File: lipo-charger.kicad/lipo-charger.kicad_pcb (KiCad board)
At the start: 2 copper layers, 23 x 35 mm, 18 parts, among them J1 JST-PH2 Device, J3 JST-PH2 Bat, U1 MCP73831-2-OT, U2 XB6166IS

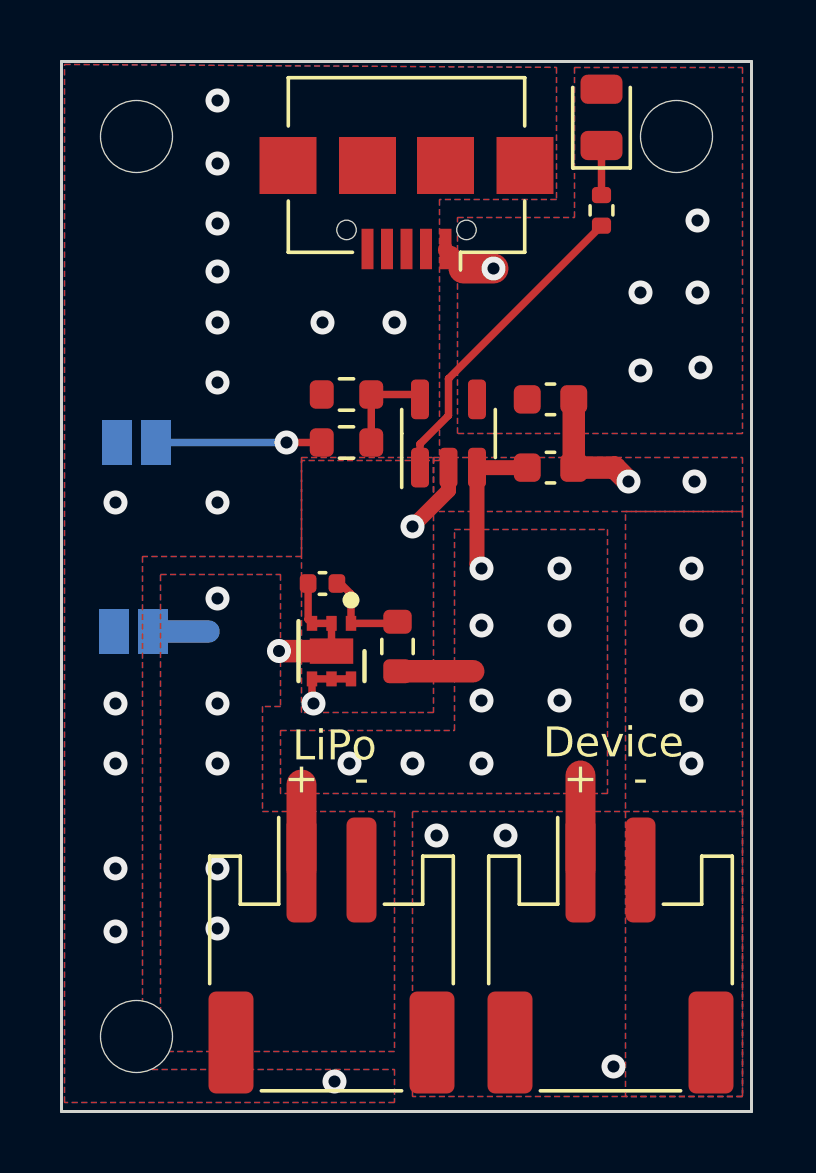
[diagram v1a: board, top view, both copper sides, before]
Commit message: Rev: 0.92: add (optional) switch for load
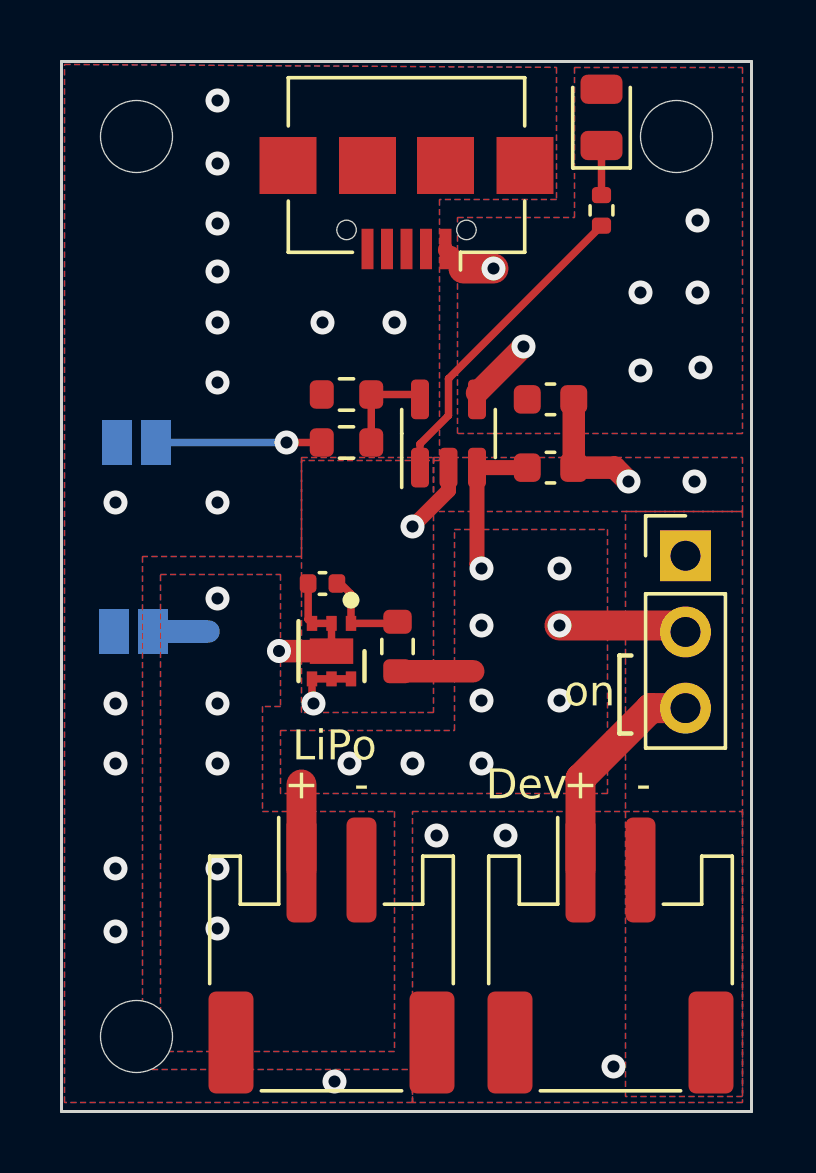
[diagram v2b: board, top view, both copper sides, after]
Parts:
- added SW1: SW_SPDT, Connector_PinHeader_2.54mm:PinHeader_1x03_P2.54mm_Vertical, F.Cu at (120.8, 116.5)
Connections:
- J1 pad 1: +BATT -> Net-(J1-Pad1)
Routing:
- net Net-(J1-Pad1): track 0.00 -> 7.52 mm
- net VBUS: track 1.90 -> 4.30 mm, vias 6 -> 7
- net +BATT: track 13.6 -> 14.8 mm
- net GND: vias 26 -> 22
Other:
- board text added: "Dev"
- board text added: "https://github.com/bablokb/ pcb-lipo-charger Rev: 0.92"
- board text added: "on"
- board text removed: "Device"
- board text removed: "https://github.com/bablokb/ pcb-lipo-charger Rev: 0.91"
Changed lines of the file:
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@@
   (net 11 "unconnected-(USB1-Pad3)")
   (net 12 "unconnected-(USB1-Pad2)")
+  (net 13 "Net-(J1-Pad1)")
+  (net 14 "unconnected-(SW1-Pad1)")
   (footprint "user:MountingHole_2.4mm_M2" (layer "F.Cu")
     (at 120.5 102.5)
@@
     )
   )
+  (footprint "Connector_PinHeader_2.54mm:PinHeader_1x03_P2.54mm_Vertical" (layer "F.Cu")
+    (at 120.8 116.475)
+    (descr "Through hole straight pin header, 1x03, 2.54mm pitch, single row")
+    (tags "Through hole pin header THT 1x03 2.54mm single row")
+    (property "Sheetfile" "lipo-charger.kicad_sch")
+    (property "Sheetname" "")
+    (attr through_hole)
+    (fp_text reference "SW1" (at 0 -2.33) (layer "F.SilkS") hide
+      (effects (font (size 1 1) (thickness 0.15)))
+    )
+    (fp_text value "SW_SPDT" (at 0 7.41) (layer "F.Fab")
+      (effects (font (size 1 1) (thickness 0.15)))
+    )
+    (fp_text user "${REFERENCE}" (at 0 2.54 90) (layer "F.Fab")
+      (effects (font (size 1 1) (thickness 0.15)))
+    )
+    (fp_line (start -1.33 6.41) (end 1.33 6.41) (layer "F.SilkS") (width 0.12))
+    (fp_line (start -1.33 -1.33) (end 0 -1.33) (layer "F.SilkS") (width 0.12))
+    (fp_line (start 1.33 1.27) (end 1.33 6.41) (layer "F.SilkS") (width 0.12))
+    (fp_line (start -1.33 0) (end -1.33 -1.33) (layer "F.SilkS") (width 0.12))
+    (fp_line (start -1.33 1.27) (end 1.33 1.27) (layer "F.SilkS") (width 0.12))
+    (fp_line (start -1.33 1.27) (end -1.33 6.41) (layer "F.SilkS") (width 0.12))
+    (fp_line (start 1.8 -1.8) (end -1.8 -1.8) (layer "F.CrtYd") (width 0.05))
+    (fp_line (start 1.8 6.85) (end 1.8 -1.8) (layer "F.CrtYd") (width 0.05))
+    (fp_line (start -1.8 6.85) (end 1.8 6.85) (layer "F.CrtYd") (width 0.05))
+    (fp_line (start -1.8 -1.8) (end -1.8 6.85) (layer "F.CrtYd") (width 0.05))
+    (fp_line (start -1.27 -0.635) (end -0.635 -1.27) (layer "F.Fab") (width 0.1))
+    (fp_line (start 1.27 -1.27) (end 1.27 6.35) (layer "F.Fab") (width 0.1))
+    (fp_line (start -0.635 -1.27) (end 1.27 -1.27) (layer "F.Fab") (width 0.1))
+    (fp_line (start 1.27 6.35) (end -1.27 6.35) (layer "F.Fab") (width 0.1))
+    (fp_line (start -1.27 6.35) (end -1.27 -0.635) (layer "F.Fab") (width 0.1))
+    (pad "1" thru_hole rect (at 0 0) (size 1.7 1.7) (drill 1) (layers *.Cu *.Mask)
+      (net 14 "unconnected-(SW1-Pad1)") (pinfunction "A") (pintype "passive+no_connect"))
+    (pad "2" thru_hole oval (at 0 2.54) (size 1.7 1.7) (drill 1) (layers *.Cu *.Mask)
+      (net 3 "+BATT") (pinfunction "B") (pintype "passive"))
+    (pad "3" thru_hole oval (at 0 5.08) (size 1.7 1.7) (drill 1) (layers *.Cu *.Mask)
+      (net 13 "Net-(J1-Pad1)") (pinfunction "C") (pintype "passive"))
+    (model "${KICAD6_3DMODEL_DIR}/Connector_PinHeader_2.54mm.3dshapes/PinHeader_1x03_P2.54mm_Vertical.wrl"
+      (offset (xyz 0 0 0))
+      (scale (xyz 1 1 1))
+      (rotate (xyz 0 0 0))
+    )
+  )
   (footprint "Resistor_SMD:R_0402_1005Metric" (layer "F.Cu")
     (at 118 104.9625 90)
@@
     (fp_line (start -3.95 -3.2) (end -3.15 -3.2) (layer "F.Fab") (width 0.1))
     (pad "1" smd roundrect (at -1 -2.85) (size 1 3.5) (layers "F.Cu" "F.Paste" "F.Mask") (roundrect_rratio 0.25)
-      (net 3 "+BATT") (pinfunction "Pin_1") (pintype "passive"))
+      (net 13 "Net-(J1-Pad1)") (pinfunction "Pin_1") (pintype "passive"))
     (pad "2" smd roundrect (at 1 -2.85) (size 1 3.5) (layers "F.Cu" "F.Paste" "F.Mask") (roundrect_rratio 0.25)
       (net 2 "GND") (pinfunction "Pin_2") (pintype "passive"))
@@
       (net 7 "Net-(JP1-Pad2)") (pinfunction "B") (pintype "passive"))
   )
+  (gr_line (start 118.6 119.8) (end 118.6 122.4) (layer "F.SilkS") (width 0.15))
+  (gr_line (start 118.6 122.4) (end 119 122.4) (layer "F.SilkS") (width 0.15))
+  (gr_line (start 118.6 119.8) (end 119 119.8) (layer "F.SilkS") (width 0.15))
   (gr_line (start 100 100) (end 123 100) (layer "Edge.Cuts") (width 0.1))
   (gr_line (start 123 100) (end 123 135) (layer "Edge.Cuts") (width 0.1))
   (gr_line (start 100 135) (end 100 100) (layer "Edge.Cuts") (width 0.1))
   (gr_line (start 123 135) (end 100 135) (layer "Edge.Cuts") (width 0.1))
-  (gr_text "https://github.com/bablokb/\n  pcb-lipo-charger\nRev: 0.91" (at 121.8 106.2) (layer "B.SilkS")
+  (gr_text "https://github.com/bablokb/\n  pcb-lipo-charger\nRev: 0.92" (at 121.8 106.2) (layer "B.SilkS")
     (effects (font (size 0.9 0.9) (thickness 0.15)) (justify left mirror))
   )
@@
     (effects (font (size 1 1) (thickness 0.15)) (justify left mirror))
   )
-  (gr_text "I charge: 200mA\nI fast:    500mA\n\nI load: 900mA max" (at 121.7 118.2) (layer "B.SilkS")
+  (gr_text "I charge: 200mA\nI fast:    500mA\n\nI load: 900mA max" (at 118.9 118.3) (layer "B.SilkS")
     (effects (font (size 1 1) (thickness 0.15)) (justify left mirror))
   )
-  (gr_text "+" (at 108 123.9) (layer "F.SilkS")
+  (gr_text "+" (at 108 124.1) (layer "F.SilkS")
     (effects (font (size 1 1) (thickness 0.15)))
   )
@@
     (effects (font (size 1 1) (thickness 0.15)))
   )
-  (gr_text "Device" (at 118.4 122.7) (layer "F.SilkS")
+  (gr_text "Dev" (at 115.5 124.1) (layer "F.SilkS")
     (effects (font (size 1 1) (thickness 0.15)))
   )
-  (gr_text "-" (at 119.3 123.9) (layer "F.SilkS")
+  (gr_text "on" (at 117.6 121) (layer "F.SilkS")
     (effects (font (size 1 1) (thickness 0.15)))
   )
-  (gr_text "-" (at 110 123.9) (layer "F.SilkS")
+  (gr_text "-" (at 119.4 124.1) (layer "F.SilkS")
     (effects (font (size 1 1) (thickness 0.15)))
   )
-  (gr_text "+" (at 117.3 123.9) (layer "F.SilkS")
+  (gr_text "-" (at 110 124.1) (layer "F.SilkS")
     (effects (font (size 1 1) (thickness 0.15)))
   )
+  (gr_text "+" (at 117.3 124.1) (layer "F.SilkS")
+    (effects (font (size 1 1) (thickness 0.15)))
+  )
+  (segment (start 113.85 111.05) (end 115.4 109.5) (width 0.75) (layer "F.Cu") (net 1))
   (segment (start 113.6 107) (end 113 106.4) (width 0.5) (layer "F.Cu") (net 1))
+  (segment (start 113.85 111.2625) (end 113.85 111.05) (width 0.25) (layer "F.Cu") (net 1))
   (segment (start 112.8 106.3) (end 112.8 106.25) (width 0.5) (layer "F.Cu") (net 1))
   (segment (start 114.4 106.9) (end 113.4 106.9) (width 1) (layer "F.Cu") (net 1))
@@
   (via (at 121.3 110.2) (size 0.8) (drill 0.4) (layers "F.Cu" "B.Cu") (free) (net 1))
   (via (at 121.2 107.7) (size 0.8) (drill 0.4) (layers "F.Cu" "B.Cu") (free) (net 1))
+  (via (at 115.4 109.5) (size 0.8) (drill 0.4) (layers "F.Cu" "B.Cu") (net 1))
   (via (at 114.4 106.9) (size 0.8) (drill 0.4) (layers "F.Cu" "B.Cu") (free) (net 1))
   (via (at 121.2 105.3) (size 0.8) (drill 0.4) (layers "F.Cu" "B.Cu") (free) (net 1))
@@
   (via (at 111.1 108.7) (size 0.8) (drill 0.4) (layers "F.Cu" "B.Cu") (free) (net 2))
   (via (at 105.2 108.7) (size 0.8) (drill 0.4) (layers "F.Cu" "B.Cu") (free) (net 2))
-  (via (at 121 116.9) (size 0.8) (drill 0.4) (layers "F.Cu" "B.Cu") (free) (net 2))
   (via (at 112.5 125.8) (size 0.8) (drill 0.4) (layers "F.Cu" "B.Cu") (free) (net 2))
-  (via (at 121 123.4) (size 0.8) (drill 0.4) (layers "F.Cu" "B.Cu") (free) (net 2))
-  (via (at 121 121.3) (size 0.8) (drill 0.4) (layers "F.Cu" "B.Cu") (free) (net 2))
   (via (at 101.8 121.4) (size 0.8) (drill 0.4) (layers "F.Cu" "B.Cu") (free) (net 2))
   (via (at 121.1 114) (size 0.8) (drill 0.4) (layers "F.Cu" "B.Cu") (free) (net 2))
@@
   (via (at 105.2 105.4) (size 0.8) (drill 0.4) (layers "F.Cu" "B.Cu") (free) (net 2))
   (via (at 118.4 133.5) (size 0.8) (drill 0.4) (layers "F.Cu" "B.Cu") (free) (net 2))
-  (via (at 121 118.8) (size 0.8) (drill 0.4) (layers "F.Cu" "B.Cu") (free) (net 2))
   (via (at 108.4 121.4) (size 0.8) (drill 0.4) (layers "F.Cu" "B.Cu") (net 2))
   (via (at 101.8 123.4) (size 0.8) (drill 0.4) (layers "F.Cu" "B.Cu") (free) (net 2))
@@
   (segment (start 111.2 120.325) (end 113.725 120.325) (width 0.75) (layer "F.Cu") (net 3))
   (segment (start 113.85 113.5375) (end 115.525 113.5375) (width 0.5) (layer "F.Cu") (net 3))
-  (segment (start 117.3 126.95) (end 117.3 123.8) (width 1) (layer "F.Cu") (net 3))
+  (segment (start 120.585 118.8) (end 120.8 119.015) (width 1) (layer "F.Cu") (net 3))
   (segment (start 108 126.95) (end 108 124.1) (width 1) (layer "F.Cu") (net 3))
+  (segment (start 116.6 118.8) (end 120.585 118.8) (width 1) (layer "F.Cu") (net 3))
   (segment (start 113.85 113.5375) (end 113.85 116.75) (width 0.5) (layer "F.Cu") (net 3))
   (via (at 109.6 123.4) (size 0.8) (drill 0.4) (layers "F.Cu" "B.Cu") (free) (net 3))
@@
   (segment (start 111.95 112.75) (end 112.9 111.8) (width 0.25) (layer "F.Cu") (net 9))
   (segment (start 111.95 113.5375) (end 111.95 112.75) (width 0.25) (layer "F.Cu") (net 9))
+  (segment (start 119.645 121.555) (end 120.8 121.555) (width 1) (layer "F.Cu") (net 13))
+  (segment (start 117.3 123.9) (end 119.645 121.555) (width 1) (layer "F.Cu") (net 13))
+  (segment (start 117.3 126.95) (end 117.3 123.9) (width 1) (layer "F.Cu") (net 13))
   (zone (net 3) (net_name "+BATT") (layers F&B.Cu) (hatch edge 0.508)
     (connect_pads (clearance 0.508))
@@
         (xy 102.7 116.5)
         (xy 102.7 133.6)
-        (xy 111.1 133.6)
-        (xy 111.1 134.7)
+        (xy 111.7 133.6)
+        (xy 111.7 134.7)
         (xy 100.1 134.7)
         (xy 100.100015 100.09756)
@@
     (polygon
       (pts
-        (xy 122.7 134.5)
-        (xy 111.7 134.5)
+        (xy 122.7 134.7)
+        (xy 111.7 134.7)
         (xy 111.7 125)
         (xy 122.7 125)

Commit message: Rev. 0.93 (added switch for load) - in production
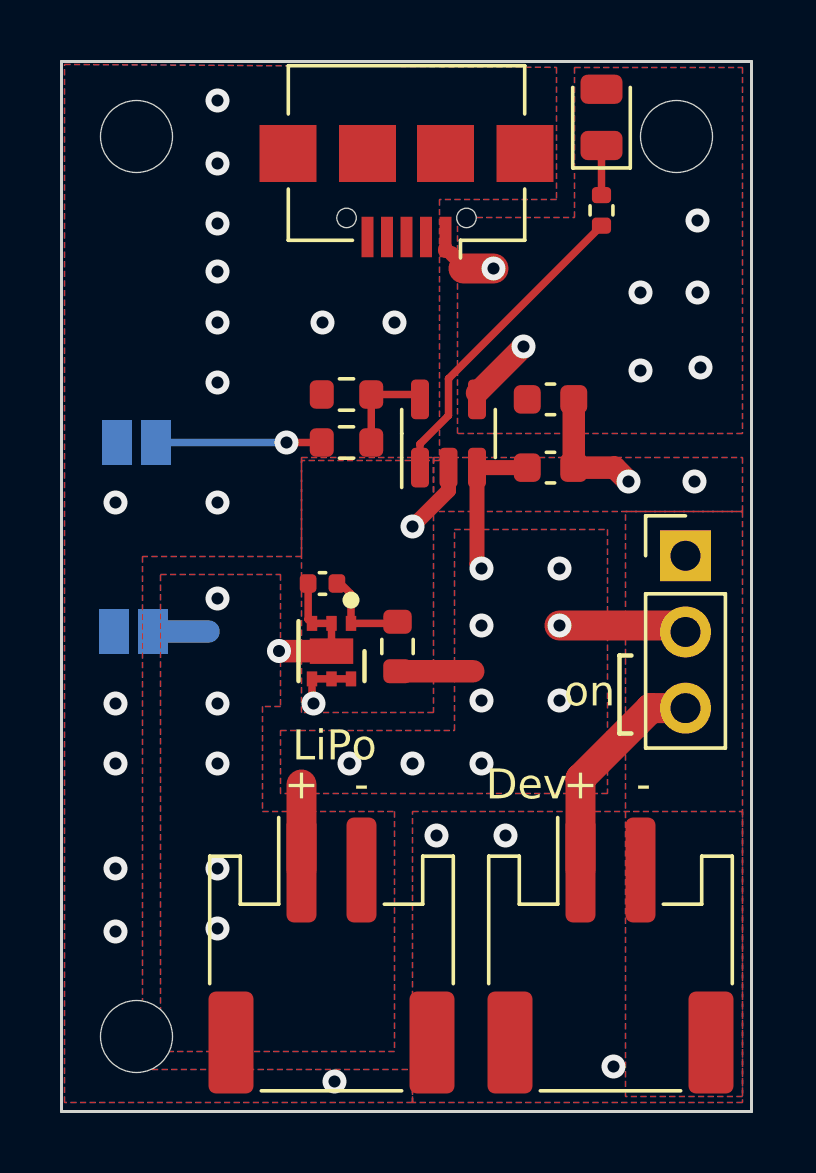
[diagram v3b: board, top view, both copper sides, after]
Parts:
- SW1: value SW_SPDT -> SW_ON
- moved USB1 0.40 mm to (111.5, 104.5)
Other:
- board text added: "https://github.com/bablokb/ pcb-lipo-charger Rev: 0.93"
- board text removed: "https://github.com/bablokb/ pcb-lipo-charger Rev: 0.92"
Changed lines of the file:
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@@
     (property "Sheetfile" "lipo-charger.kicad_sch")
     (property "Sheetname" "")
-    (attr exclude_from_pos_files)
+    (property "exclude_from_bom" "")
+    (attr exclude_from_pos_files exclude_from_bom)
     (fp_text reference "H2" (at 0 -3.2) (layer "F.SilkS") hide
       (effects (font (size 1 1) (thickness 0.15)))
@@
     (property "Sheetfile" "lipo-charger.kicad_sch")
     (property "Sheetname" "")
-    (attr exclude_from_pos_files)
+    (property "exclude_from_bom" "")
+    (attr exclude_from_pos_files exclude_from_bom)
     (fp_text reference "H3" (at 0 -3.2) (layer "F.SilkS") hide
       (effects (font (size 1 1) (thickness 0.15)))
@@
   )
   (footprint "user:USB_Micro-B_JLCPCB_40942" (layer "F.Cu")
-    (at 111.5 104.858 180)
+    (at 111.5 104.458 180)
     (descr "USB Micro-B, horizontal, https://datasheet.lcsc.com/szlcsc/2103081232_Jing-Extension-of-the-Electronic-Co-920-D62A2021S10100_C40942.pdf")
     (tags "USB Micro B horizontal")
@@
       (effects (font (size 1 1) (thickness 0.15)))
     )
-    (fp_text user "PCB edge" (at 0 2.733) (layer "Dwgs.User") hide
+    (fp_text user "PCB edge" (at 0 2.733) (layer "Dwgs.User")
       (effects (font (size 0.5 0.5) (thickness 0.08)))
     )
@@
     (descr "SOT, 5 Pin (https://www.jedec.org/sites/default/files/docs/Mo-178c.PDF variant AA), generated with kicad-footprint-generator ipc_gullwing_generator.py")
     (tags "SOT TO_SOT_SMD")
-    (property "LCSC" " C424093 ")
+    (property "LCSC" "C424093")
     (property "Sheetfile" "lipo-charger.kicad_sch")
     (property "Sheetname" "")
@@
     (property "Sheetfile" "lipo-charger.kicad_sch")
     (property "Sheetname" "")
-    (attr through_hole)
+    (property "exclude_from_bom" "")
+    (attr through_hole exclude_from_pos_files exclude_from_bom)
     (fp_text reference "SW1" (at 0 -2.33) (layer "F.SilkS") hide
       (effects (font (size 1 1) (thickness 0.15)))
     )
-    (fp_text value "SW_SPDT" (at 0 7.41) (layer "F.Fab")
+    (fp_text value "SW_ON" (at 0 7.41) (layer "F.Fab")
       (effects (font (size 1 1) (thickness 0.15)))
     )
@@
     (pad "2" smd roundrect (at 1 -2.85) (size 1 3.5) (layers "F.Cu" "F.Paste" "F.Mask") (roundrect_rratio 0.25)
       (net 2 "GND") (pinfunction "Pin_2") (pintype "passive"))
-    (pad "MP" smd roundrect (at 3.35 2.9) (size 1.5 3.4) (layers "F.Cu" "F.Paste" "F.Mask") (roundrect_rratio 0.166667))
-    (pad "MP" smd roundrect (at -3.35 2.9) (size 1.5 3.4) (layers "F.Cu" "F.Paste" "F.Mask") (roundrect_rratio 0.166667))
+    (pad "MP" smd roundrect (at 3.35 2.9) (size 1.5 3.4) (layers "F.Cu" "F.Paste" "F.Mask") (roundrect_rratio 0.1666673333))
+    (pad "MP" smd roundrect (at -3.35 2.9) (size 1.5 3.4) (layers "F.Cu" "F.Paste" "F.Mask") (roundrect_rratio 0.1666673333))
     (model "${KICAD6_3DMODEL_DIR}/Connector_JST.3dshapes/JST_PH_S2B-PH-SM4-TB_1x02-1MP_P2.00mm_Horizontal.wrl"
       (offset (xyz 0 0 0))
@@
     (pad "2" smd roundrect (at 1 -2.85) (size 1 3.5) (layers "F.Cu" "F.Paste" "F.Mask") (roundrect_rratio 0.25)
       (net 5 "-BATT") (pinfunction "Pin_2") (pintype "passive"))
-    (pad "MP" smd roundrect (at 3.35 2.9) (size 1.5 3.4) (layers "F.Cu" "F.Paste" "F.Mask") (roundrect_rratio 0.166667))
-    (pad "MP" smd roundrect (at -3.35 2.9) (size 1.5 3.4) (layers "F.Cu" "F.Paste" "F.Mask") (roundrect_rratio 0.166667))
+    (pad "MP" smd roundrect (at 3.35 2.9) (size 1.5 3.4) (layers "F.Cu" "F.Paste" "F.Mask") (roundrect_rratio 0.1666673333))
+    (pad "MP" smd roundrect (at -3.35 2.9) (size 1.5 3.4) (layers "F.Cu" "F.Paste" "F.Mask") (roundrect_rratio 0.1666673333))
     (model "${KICAD6_3DMODEL_DIR}/Connector_JST.3dshapes/JST_PH_S2B-PH-SM4-TB_1x02-1MP_P2.00mm_Horizontal.wrl"
       (offset (xyz 0 0 0))
@@
     (descr "Resistor SMD 0603 (1608 Metric), square (rectangular) end terminal, IPC_7351 nominal, (Body size source: IPC-SM-782 page 72, https://www.pcb-3d.com/wordpress/wp-content/uploads/ipc-sm-782a_amendment_1_and_2.pdf), generated with kicad-footprint-generator")
     (tags "resistor")
-    (property "LCSC" "C23046")
+    (property "LCSC" "C21190")
     (property "Sheetfile" "lipo-charger.kicad_sch")
     (property "Sheetname" "")
@@
     (property "Sheetfile" "lipo-charger.kicad_sch")
     (property "Sheetname" "")
-    (attr exclude_from_pos_files)
+    (property "exclude_from_bom" "")
+    (attr exclude_from_pos_files exclude_from_bom)
     (fp_text reference "H1" (at 0 -3.2) (layer "F.SilkS") hide
       (effects (font (size 1 1) (thickness 0.15)))
@@
     (property "Sheetfile" "lipo-charger.kicad_sch")
     (property "Sheetname" "")
-    (attr exclude_from_pos_files)
+    (property "exclude_from_bom" "")
+    (attr exclude_from_pos_files exclude_from_bom)
     (fp_text reference "JP2" (at 0 1.8) (layer "B.SilkS") hide
       (effects (font (size 1 1) (thickness 0.15)) (justify mirror))
@@
     (property "Sheetfile" "lipo-charger.kicad_sch")
     (property "Sheetname" "")
-    (attr exclude_from_pos_files)
+    (property "exclude_from_bom" "")
+    (attr exclude_from_pos_files exclude_from_bom)
     (fp_text reference "JP1" (at 0.05 2.05) (layer "B.SilkS") hide
       (effects (font (size 1 1) (thickness 0.15)) (justify mirror))
@@
   (gr_line (start 100 135) (end 100 100) (layer "Edge.Cuts") (width 0.1))
   (gr_line (start 123 135) (end 100 135) (layer "Edge.Cuts") (width 0.1))
-  (gr_text "https://github.com/bablokb/\n  pcb-lipo-charger\nRev: 0.92" (at 121.8 106.2) (layer "B.SilkS")
+  (gr_text "https://github.com/bablokb/\n  pcb-lipo-charger\nRev: 0.93" (at 122.1 107.4) (layer "B.SilkS")
     (effects (font (size 0.9 0.9) (thickness 0.15)) (justify left mirror))
   )
-  (gr_text "No\nProtect" (at 102.4 120.3 270) (layer "B.SilkS")
+  (gr_text "No\nProtect" (at 104.4 118.9) (layer "B.SilkS")
     (effects (font (size 1 1) (thickness 0.15)) (justify right mirror))
   )
-  (gr_text "Fast\nCharge" (at 102.65 111.3 270) (layer "B.SilkS")
+  (gr_text "Fast\nCharge" (at 104.4 112.5) (layer "B.SilkS")
+    (effects (font (size 1 1) (thickness 0.15)) (justify right mirror))
+  )
+  (gr_text "I charge: 200mA\nI fast:    500mA\n\nI load: 900mA max" (at 121.9 128.9) (layer "B.SilkS")
     (effects (font (size 1 1) (thickness 0.15)) (justify left mirror))
   )
-  (gr_text "I charge: 200mA\nI fast:    500mA\n\nI load: 900mA max" (at 118.9 118.3) (layer "B.SilkS")
-    (effects (font (size 1 1) (thickness 0.15)) (justify left mirror))
-  )
